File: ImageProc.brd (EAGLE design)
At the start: 49.8 x 23.2 mm, 117 parts, among them IC1 XC61GC3002HR-G, IC10 AT45DB642D-CNU, IC2 MIC5335-SPYMT, IC3 MIC5335-JGYMT, IC4 DSPIC33FJ128MC706A, IC5 AT86RF233-ZU, IC6 LTC6088, IC7 DRV8833RTY, IC8 DRV8833RTY, IC9 MPU-6000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

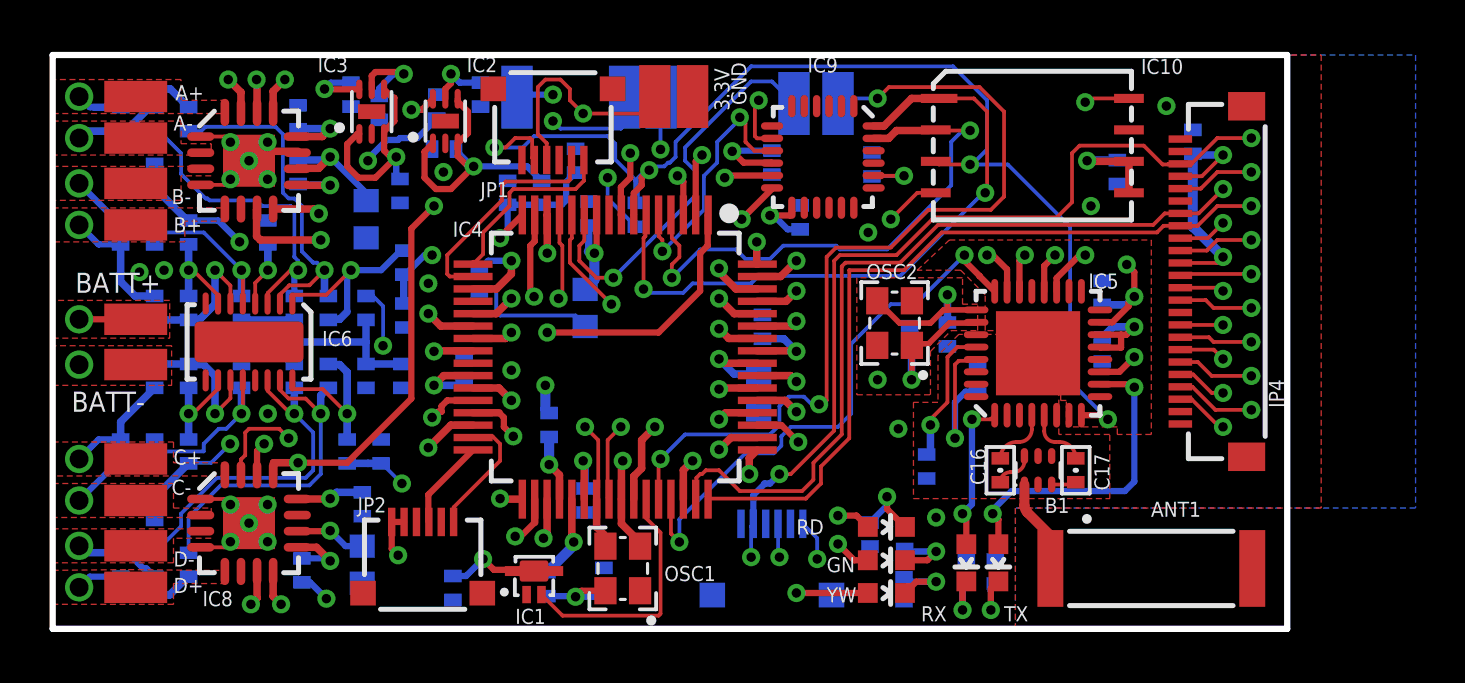
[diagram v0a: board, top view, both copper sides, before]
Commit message: Fixed many of 2.5 A's erratta, to form 2.5B.
Fixed the top motor controller's missing GND pin.

Fixed the Radio Chip's pins that were combined.

Fixed C37/C40 mislabeling.
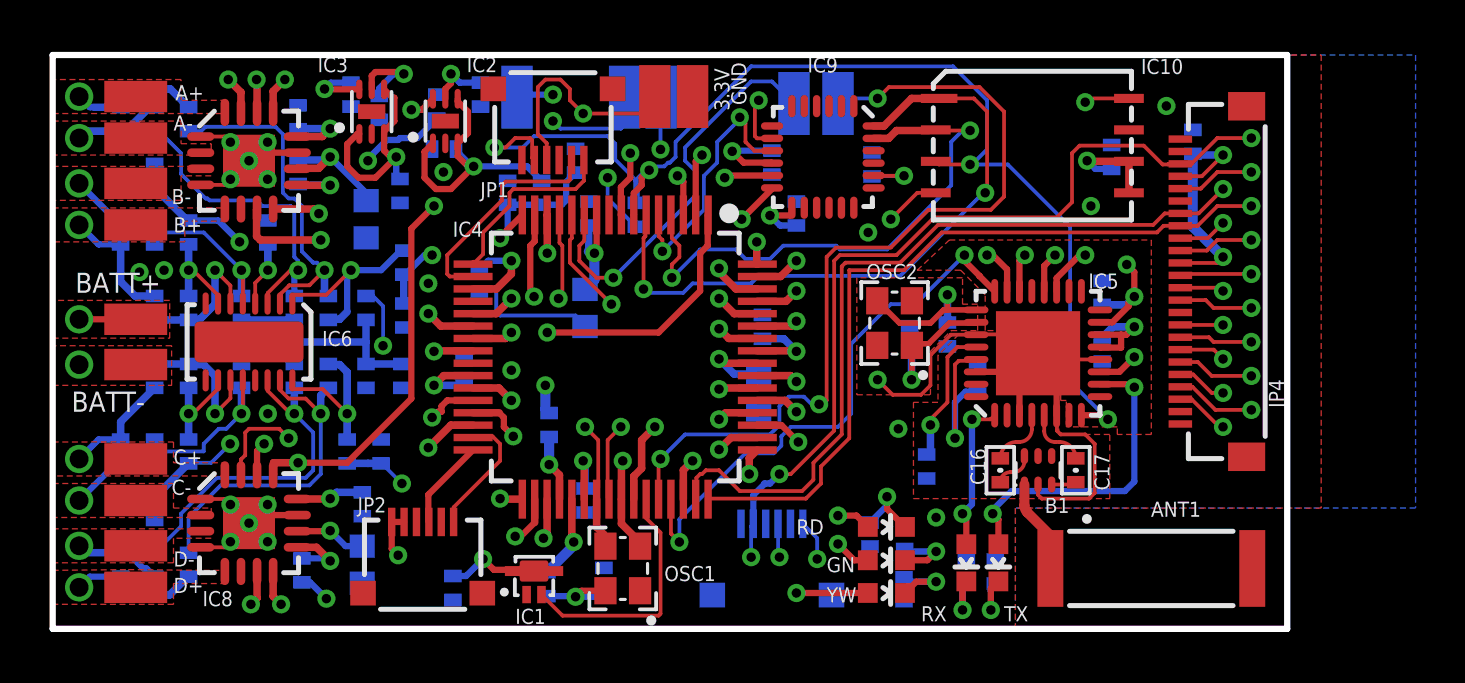
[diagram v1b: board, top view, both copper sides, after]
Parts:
- moved C37 13.1 mm to (30.0, 16.8), turned to 90 degrees
- moved C40 12.8 mm to (42.7, 19.1)
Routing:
- net GND: track 14.7 -> 45.1 mm

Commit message: Added Pads for PWM 1 and 2 to MOTOR_C_IN_2 and MOTOR_D_IN_2 on the top.
Added this both to the schematic and routed it on the board.
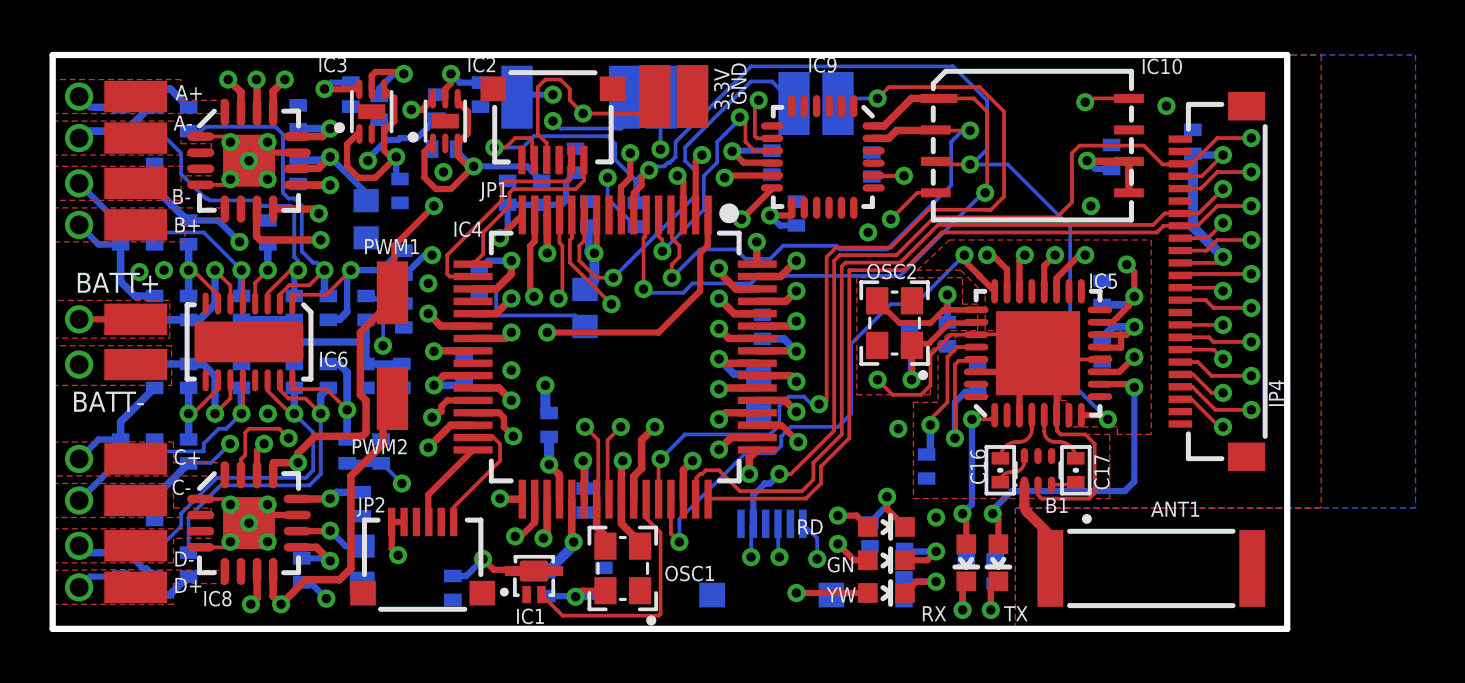
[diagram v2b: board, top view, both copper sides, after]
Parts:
- added PWM1, PWM2: EXT5, wirepad:SMD1,27-2,54
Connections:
- net MOTOR_C_IN2: now also PWM1.1
- net MOTOR_D_IN2: now also PWM2.1
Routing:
- net MOTOR_D_IN2: track 34.6 -> 45.6 mm

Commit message: Update PCB date, correct bridge on AT86RF233
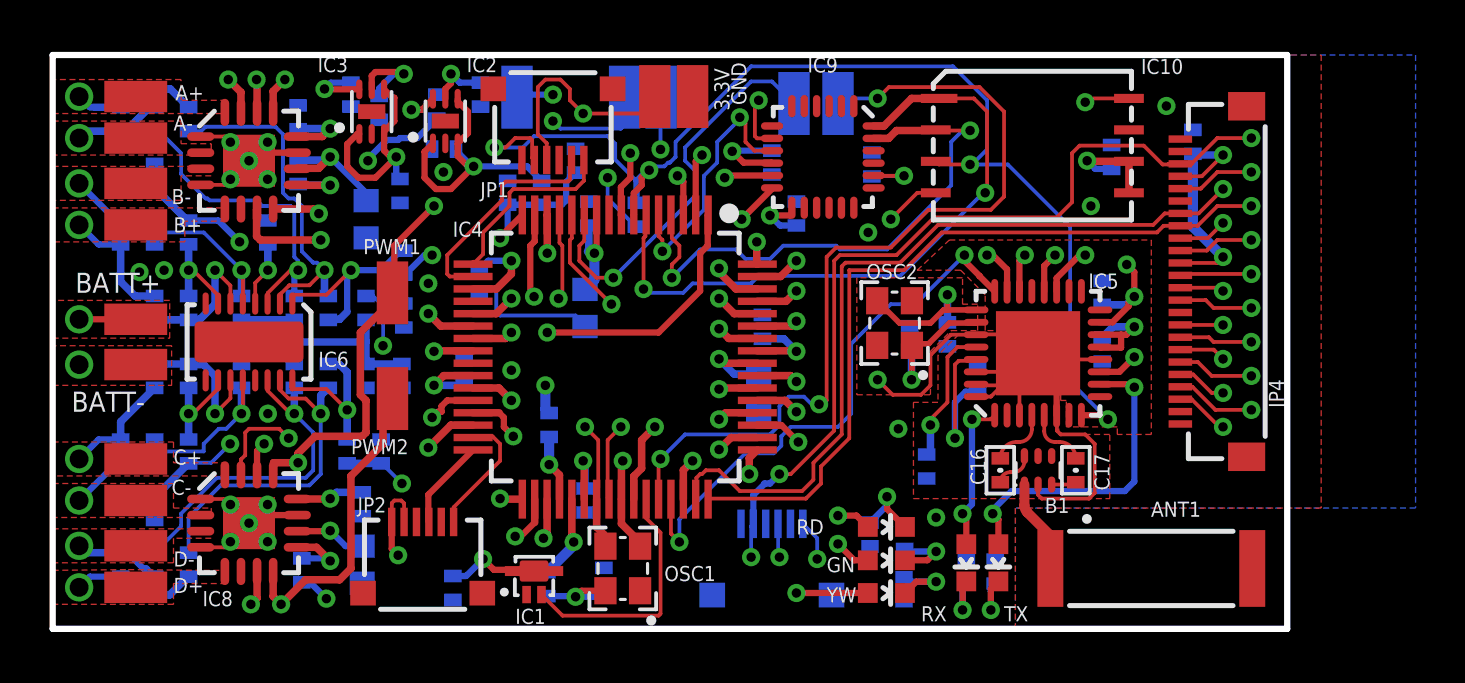
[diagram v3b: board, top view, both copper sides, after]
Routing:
- net GND: track 45.1 -> 48.0 mm
- net V_BATT: track 42.9 -> 44.5 mm
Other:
- board text added: "2012.08.18"
- board text removed: "2012.07.26"
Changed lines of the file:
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@@
 <setting verticaltext="up"/>
 </settings>
-<grid distance="3" unitdist="mil" unit="mil" style="lines" multiple="1" display="yes" altdistance="1" altunitdist="mil" altunit="mil"/>
+<grid distance="1" unitdist="mil" unit="mil" style="lines" multiple="1" display="yes" altdistance="1" altunitdist="mil" altunit="mil"/>
 <layers>
 <layer number="1" name="Top" color="4" fill="1" visible="yes" active="yes"/>
@@
 <layer number="21" name="tPlace" color="16" fill="1" visible="no" active="yes"/>
 <layer number="22" name="bPlace" color="14" fill="1" visible="no" active="yes"/>
-<layer number="23" name="tOrigins" color="15" fill="1" visible="yes" active="yes"/>
+<layer number="23" name="tOrigins" color="15" fill="1" visible="no" active="yes"/>
 <layer number="24" name="bOrigins" color="15" fill="1" visible="no" active="yes"/>
-<layer number="25" name="tNames" color="7" fill="1" visible="yes" active="yes"/>
+<layer number="25" name="tNames" color="7" fill="1" visible="no" active="yes"/>
 <layer number="26" name="bNames" color="7" fill="1" visible="no" active="yes"/>
 <layer number="27" name="tValues" color="7" fill="1" visible="yes" active="yes"/>
-<layer number="28" name="bValues" color="7" fill="1" visible="no" active="yes"/>
+<layer number="28" name="bValues" color="7" fill="1" visible="yes" active="yes"/>
 <layer number="29" name="tStop" color="7" fill="3" visible="yes" active="yes"/>
 <layer number="30" name="bStop" color="7" fill="6" visible="no" active="yes"/>
@@
 <layer number="37" name="tTest" color="7" fill="1" visible="no" active="yes"/>
 <layer number="38" name="bTest" color="7" fill="1" visible="no" active="yes"/>
-<layer number="39" name="tKeepout" color="4" fill="11" visible="no" active="yes"/>
+<layer number="39" name="tKeepout" color="4" fill="11" visible="yes" active="yes"/>
 <layer number="40" name="bKeepout" color="1" fill="11" visible="no" active="yes"/>
-<layer number="41" name="tRestrict" color="4" fill="10" visible="no" active="yes"/>
+<layer number="41" name="tRestrict" color="4" fill="10" visible="yes" active="yes"/>
 <layer number="42" name="bRestrict" color="1" fill="10" visible="no" active="yes"/>
 <layer number="43" name="vRestrict" color="2" fill="10" visible="no" active="yes"/>
@@
 <text x="49.370025" y="5.628090625" size="0.6096" layer="22" font="vector" ratio="25" rot="MR0">Douglas Hutchings</text>
 <text x="49.3776" y="6.5532" size="0.6096" layer="22" font="vector" ratio="25" rot="MR0">Ryan Julian</text>
-<text x="49.3776" y="1.3716" size="0.6096" layer="22" font="vector" ratio="25" rot="MR0">2012.07.26</text>
+<text x="49.3776" y="1.3716" size="0.6096" layer="22" font="vector" ratio="25" rot="MR0">2012.08.18</text>
 <text x="49.3776" y="0.4572" size="0.6096" layer="22" font="vector" ratio="25" rot="MR0">ImageProc 2.5 Rev. B</text>
 <text x="49.3776" y="4.4196" size="0.6096" layer="22" font="vector" ratio="25" rot="MR0">Biomimetic</text>
@@
 <rectangle x1="41.36044375" y1="5.22815" x2="41.509425" y2="5.2303375" layer="22" rot="R180"/>
 <text x="42.2148" y="1.524" size="0.6096" layer="22" font="vector" ratio="25" rot="MR0">BEARS!</text>
+<wire x1="37.1856" y1="10.1346" x2="37.338" y2="10.1346" width="0" layer="41"/>
+<wire x1="37.1856" y1="9.6012" x2="37.338" y2="9.6012" width="0" layer="41"/>
 </plain>
 <attributes>
@@
 <attribute name="REVISION" value="B" x="13.716" y="13.5636" size="1.778" layer="27" rot="R180" display="off"/>
 <attribute name="YEAR" value="2012" x="13.716" y="13.5636" size="1.778" layer="27" rot="R180" display="off"/>
-<attribute name="NAME" x="12.5352" y="15.1256" size="0.6096" layer="25" ratio="25"/>
+<attribute name="NAME" x="12.5352" y="15.1256" size="0.6096" layer="25" font="vector" ratio="25"/>
 <attribute name="PWM1" value="MOTOR_C_IN_2" x="13.716" y="13.5636" size="1.778" layer="27" rot="R180" display="off"/>
 </element>
@@
 <attribute name="REVISION" value="B" x="13.716" y="9.2964" size="1.778" layer="27" rot="R180" display="off"/>
 <attribute name="YEAR" value="2012" x="13.716" y="9.2964" size="1.778" layer="27" rot="R180" display="off"/>
-<attribute name="NAME" x="14.3634" y="7.6582" size="0.6096" layer="25" ratio="25" rot="R180"/>
+<attribute name="NAME" x="14.3634" y="7.6582" size="0.6096" layer="25" font="vector" ratio="25" rot="R180"/>
 <attribute name="PWM2" value="MOTOR_D_IN_2" x="13.716" y="9.2964" size="1.778" layer="27" rot="R180" display="off"/>
 </element>
@@
 <wire x1="9.8748" y1="19.2226" x2="7.9248" y2="19.2226" width="0.254" layer="1"/>
 <wire x1="7.9248" y1="19.2226" x2="7.9248" y2="18.8976" width="0.4064" layer="1"/>
-<wire x1="37.2764" y1="10.3752" x2="39.7764" y2="10.3752" width="0.254" layer="1"/>
+<wire x1="37.2764" y1="10.3752" x2="38.2524" y2="10.3752" width="0.1524" layer="1"/>
+<wire x1="38.2524" y1="10.3752" x2="39.7764" y2="10.3752" width="0.1524" layer="1"/>
 <wire x1="39.7764" y1="10.3752" x2="39.7764" y2="10.8966" width="0.254" layer="1"/>
 <wire x1="39.7764" y1="10.8966" x2="39.7764" y2="11.1252" width="0.254" layer="1"/>
-<wire x1="39.0264" y1="8.6252" x2="39.0264" y2="10.3752" width="0.254" layer="1"/>
+<wire x1="39.0264" y1="8.6252" x2="39.0264" y2="10.3752" width="0.1524" layer="1"/>
 <wire x1="39.0264" y1="10.3752" x2="39.7764" y2="11.1252" width="0.254" layer="1"/>
 <wire x1="40.5264" y1="8.6252" x2="40.5264" y2="10.3752" width="0.254" layer="1"/>
@@
 <wire x1="9.8748" y1="4.5922" x2="8.2498" y2="4.5922" width="0.254" layer="1"/>
 <wire x1="8.2498" y1="4.5922" x2="7.9248" y2="4.2672" width="0.254" layer="1"/>
+<wire x1="38.2832" y1="9.8752" x2="38.3286" y2="9.8298" width="0.1524" layer="1"/>
+<wire x1="37.2764" y1="9.3752" x2="37.874" y2="9.3752" width="0.1524" layer="1"/>
+<wire x1="37.874" y1="9.3752" x2="38.3286" y2="9.8298" width="0.1524" layer="1"/>
+<wire x1="38.2524" y1="9.8298" x2="38.3286" y2="9.8298" width="0.1524" layer="1"/>
+<wire x1="37.2764" y1="9.8752" x2="37.3218" y2="9.8298" width="0.1524" layer="1"/>
+<wire x1="37.3218" y1="9.8298" x2="38.2524" y2="9.8298" width="0.1524" layer="1"/>
+<wire x1="38.2524" y1="9.8298" x2="38.2524" y2="10.3752" width="0.1524" layer="1"/>
 </signal>
 <signal name="SCL1">
@@
 <via x="13.9446" y="2.9718" extent="1-16" drill="0.381"/>
 <via x="17.3736" y="2.8194" extent="1-16" drill="0.381"/>
-<wire x1="13.6852" y1="4.3158" x2="14.1852" y2="4.3158" width="0.254" layer="1"/>
 <wire x1="13.6852" y1="4.3158" x2="13.6852" y2="3.2312" width="0.254" layer="1"/>
 <wire x1="13.6852" y1="3.2312" x2="13.9446" y2="2.9718" width="0.254" layer="1"/>
@@
 <wire x1="16.2814" y1="19.3675" x2="16.2941" y2="19.3675" width="0.1524" layer="16"/>
 <wire x1="16.2941" y1="19.3675" x2="16.9926" y2="18.669" width="0.1524" layer="16"/>
+<wire x1="14.1732" y1="4.3278" x2="14.1852" y2="4.3158" width="0.1524" layer="1"/>
+<wire x1="14.1852" y1="4.3158" x2="14.1852" y2="5.068" width="0.1524" layer="1"/>
+<wire x1="14.1852" y1="5.068" x2="14.0716" y2="5.1816" width="0.1524" layer="1"/>
+<wire x1="14.0716" y1="5.1816" x2="13.7922" y2="5.1816" width="0.1524" layer="1"/>
+<wire x1="13.7922" y1="5.1816" x2="13.6906" y2="5.08" width="0.1524" layer="1"/>
+<wire x1="13.6906" y1="5.08" x2="13.6906" y2="4.3212" width="0.1524" layer="1"/>
+<wire x1="13.6906" y1="4.3212" x2="13.6852" y2="4.3158" width="0.1524" layer="1"/>
 </signal>
 <signal name="N$10">
@@
 </signal>
 </signals>
-<errors>
-</errors>
 </board>
 </drawing>
